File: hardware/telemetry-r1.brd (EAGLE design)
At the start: 63.5 x 63.5 mm, 113 parts, among them IC1 COPERNICUSSMD, IC10 TPS70933, IC2 TPS70933, IC3 74HC137, IC4 STM32L073CZT6, IC5 TPS62160, IC6 HX1, IC7 LMP7702, IC8 ADXL345, IC9 HIH9131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

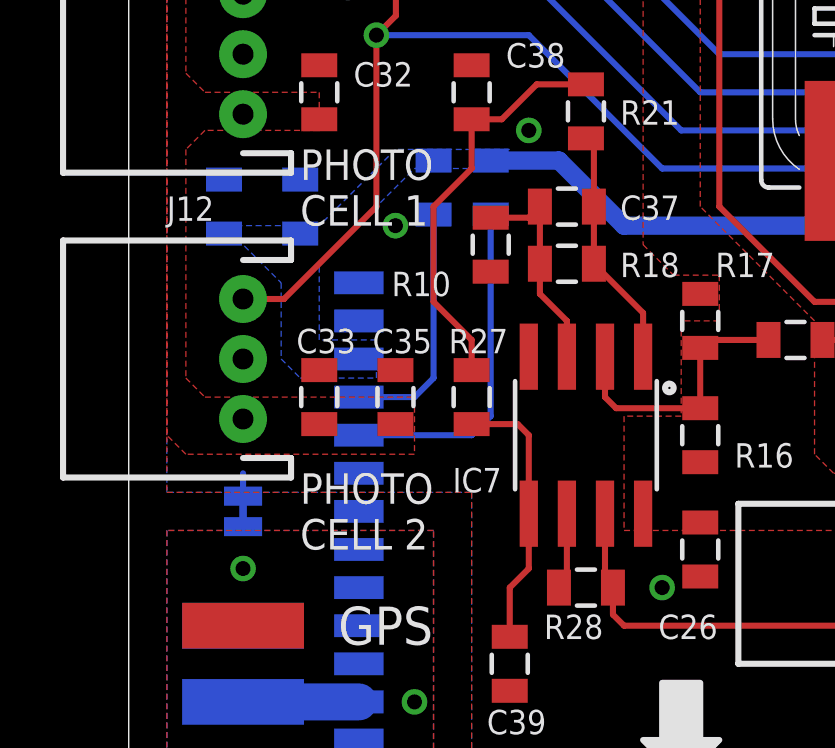
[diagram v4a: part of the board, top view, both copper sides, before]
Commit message: renamed ADC ports to use GoPro4/2 is running photo sensors
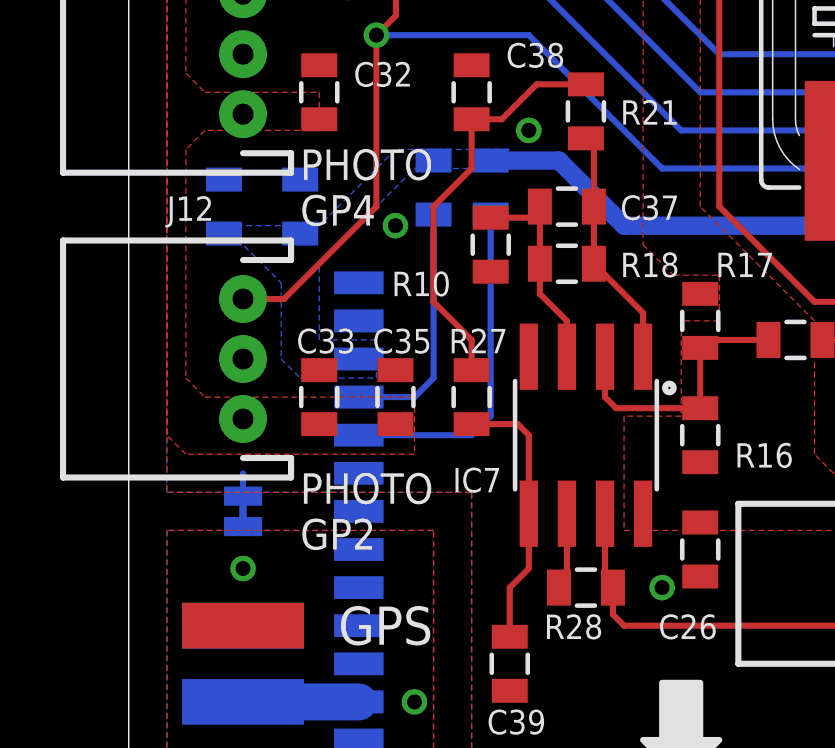
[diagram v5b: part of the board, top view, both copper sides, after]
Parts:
- J12: value INSOL -> PHOTO_GP2
- J9: value TEMP_HOT -> PHOTO_GP4
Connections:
- net INSOL renamed PHOTO_GP2
- net PHOTO renamed PHOTO_GP4
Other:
- board text added: "PHOTO GP2"
- board text added: "PHOTO GP4"
- board text removed: "PHOTO CELL 1"
- board text removed: "PHOTO CELL 2"
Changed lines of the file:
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@@
 <?xml version="1.0" encoding="utf-8"?>
 <!DOCTYPE eagle SYSTEM "eagle.dtd">
-<eagle version="7.6.0">
+<eagle version="7.5.0">
 <drawing>
 <settings>
@@
 GPS</text>
 <text x="5.715" y="22.225" size="1.016" layer="21" font="vector" ratio="10">PHOTO
-CELL 1</text>
+GP4</text>
 <text x="7.62" y="39.37" size="1.016" layer="21" font="vector" ratio="10">TEMP
 BATT</text>
 <text x="5.715" y="11.43" size="1.016" layer="21" font="vector" ratio="10">PHOTO
-CELL 2</text>
+GP2</text>
 <text x="16.51" y="61.595" size="1.27" layer="21" font="vector" ratio="10">9V</text>
 <text x="19.685" y="60.325" size="1.778" layer="21" font="vector" ratio="10">+</text>
@@
 <attribute name="NAME" x="46.355" y="13.208" size="0.8128" layer="25" font="vector"/>
 </element>
-<element name="J12" library="SparkFun-Connectors" package="JST-3-PTH" value="INSOL" x="3.81" y="17.78" smashed="yes" rot="R90">
+<element name="J12" library="SparkFun-Connectors" package="JST-3-PTH" value="PHOTO_GP2" x="3.81" y="17.78" smashed="yes" rot="R90">
 <attribute name="SKU" value="PRT-09915" x="3.81" y="17.78" size="1.778" layer="27" rot="R90" display="off"/>
 <attribute name="NAME" x="1.27" y="22.385" size="0.8128" layer="25"/>
@@
 <attribute name="VALUE" x="1.11" y="46.355" size="0.6096" layer="27" rot="R90"/>
 </element>
-<element name="J9" library="SparkFun-Connectors" package="JST-3-PTH" value="TEMP_HOT" x="3.81" y="27.94" smashed="yes" rot="R90">
+<element name="J9" library="SparkFun-Connectors" package="JST-3-PTH" value="PHOTO_GP4" x="3.81" y="27.94" smashed="yes" rot="R90">
 <attribute name="SKU" value="PRT-09915" x="3.81" y="27.94" size="1.778" layer="27" rot="R90" display="off"/>
 <attribute name="NAME" x="1.27" y="32.545" size="0.8128" layer="25"/>
@@
 <via x="60.325" y="3.81" extent="1-16" drill="0.5"/>
 </signal>
-<signal name="INSOL">
+<signal name="PHOTO_GP2">
 <contactref element="J12" pad="3"/>
 <contactref element="D6" pad="3"/>
@@
 <wire x1="43.37" y1="52.705" x2="40.83" y2="55.245" width="0.2032" layer="16"/>
 </signal>
-<signal name="PHOTO">
+<signal name="PHOTO_GP4">
 <contactref element="IC4" pad="12"/>
 <contactref element="J9" pad="3"/>

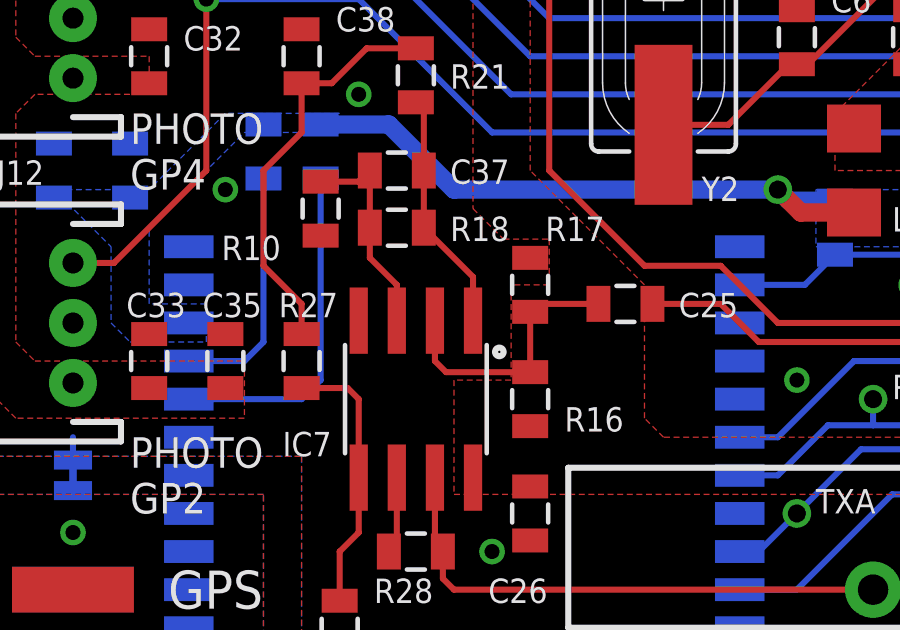
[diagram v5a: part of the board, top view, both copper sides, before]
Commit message: Fixed swapped pins in DAC filter
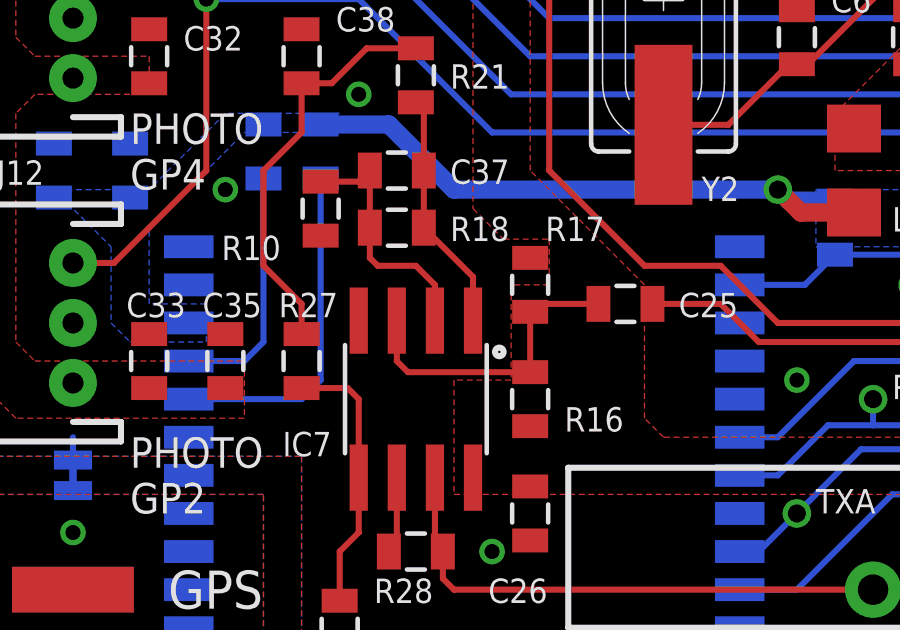
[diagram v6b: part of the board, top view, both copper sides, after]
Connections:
- net A+: now also IC7.3; no longer IC7.2
- net A-: now also IC7.2; no longer IC7.3
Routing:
- net A-: track 7.17 -> 8.44 mm
- net A+: track 9.07 -> 10.3 mm
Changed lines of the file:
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@@
 </signal>
 <signal name="A-">
-<contactref element="IC7" pad="3"/>
 <contactref element="R10" pad="2"/>
 <contactref element="C37" pad="2"/>
 <contactref element="R18" pad="1"/>
 <wire x1="13.705" y1="20.955" x2="13.705" y2="22.86" width="0.2032" layer="1"/>
-<wire x1="14.605" y1="17.8562" x2="14.605" y2="19.05" width="0.2032" layer="1"/>
-<wire x1="14.605" y1="19.05" x2="13.705" y2="19.95" width="0.2032" layer="1"/>
-<wire x1="13.705" y1="20.955" x2="13.705" y2="19.95" width="0.2032" layer="1"/>
 <wire x1="12.065" y1="22.49" x2="13.335" y2="22.49" width="0.2032" layer="1"/>
 <wire x1="13.335" y1="22.49" x2="13.705" y2="22.86" width="0.2032" layer="1"/>
+<contactref element="IC7" pad="2"/>
+<wire x1="15.875" y1="17.8562" x2="15.875" y2="19.05" width="0.2032" layer="1"/>
+<wire x1="15.875" y1="19.05" x2="15.24" y2="19.685" width="0.2032" layer="1"/>
+<wire x1="15.24" y1="19.685" x2="13.97" y2="19.685" width="0.2032" layer="1"/>
+<wire x1="13.705" y1="20.955" x2="13.705" y2="19.95" width="0.2032" layer="1"/>
+<wire x1="13.705" y1="19.95" x2="13.97" y2="19.685" width="0.2032" layer="1"/>
 </signal>
 <signal name="A+">
@@
 <contactref element="R16" pad="1"/>
 <contactref element="C25" pad="2"/>
-<contactref element="IC7" pad="2"/>
 <wire x1="21.325" y1="18.415" x2="19.315" y2="18.415" width="0.2032" layer="1"/>
 <wire x1="19.315" y1="18.415" x2="19.05" y2="18.15" width="0.2032" layer="1"/>
 <wire x1="19.05" y1="18.15" x2="19.05" y2="16.14" width="0.2032" layer="1"/>
-<wire x1="15.875" y1="17.8562" x2="15.875" y2="16.51" width="0.2032" layer="1"/>
-<wire x1="19.05" y1="16.14" x2="16.245" y2="16.14" width="0.2032" layer="1"/>
-<wire x1="16.245" y1="16.14" x2="15.875" y2="16.51" width="0.2032" layer="1"/>
+<wire x1="19.05" y1="16.14" x2="14.975" y2="16.14" width="0.2032" layer="1"/>
+<contactref element="IC7" pad="3"/>
+<wire x1="14.975" y1="16.14" x2="14.605" y2="16.51" width="0.2032" layer="1"/>
+<wire x1="14.605" y1="16.51" x2="14.605" y2="17.8562" width="0.2032" layer="1"/>
 </signal>
 <signal name="VCORE">
